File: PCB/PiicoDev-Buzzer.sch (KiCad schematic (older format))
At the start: 23 parts, among them J1 , J2 , SW1 ADDR, U1 ATtiny806

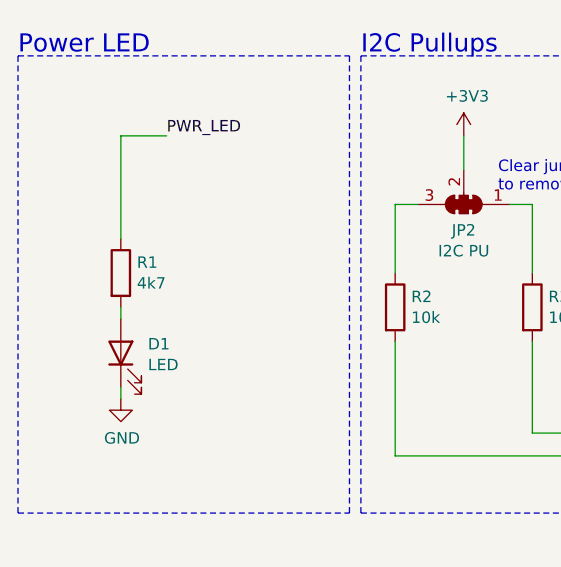
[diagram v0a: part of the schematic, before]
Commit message: Change R1 to 10k
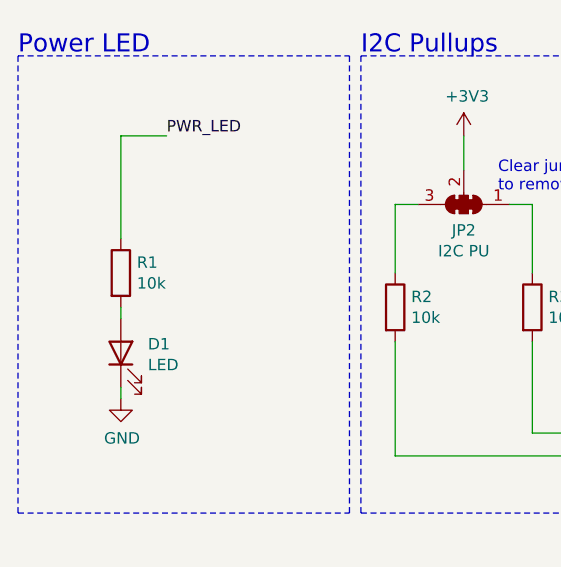
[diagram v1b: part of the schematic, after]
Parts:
- R1: value 4k7 -> 10k
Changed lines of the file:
@@
 P 1450 3950
 F 0 "R1" H 1520 3996 50  0000 L CNN
-F 1 "4k7" H 1520 3905 50  0000 L CNN
+F 1 "10k" H 1520 3905 50  0000 L CNN
 F 2 "Resistor_SMD:R_0402_1005Metric" V 1380 3950 50  0001 C CNN
 F 3 "~" H 1450 3950 50  0001 C CNN
